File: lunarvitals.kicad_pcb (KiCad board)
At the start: 2 copper layers, 48.5 x 35 mm, 38 parts, among them J1 ConductiveCord, J2 MPU6050, J3 SEN11574, J4 MAX30102, J5 USB_C_Receptacle_PowerOnly_6P, J6 Battery, J7 Conn_01x07, Q1 FS8205, SW1 SW_SPDT, U1 NRF52840-DONGLE, U3 AP2112K-3.3, U4 TP4056, U5 MLX90614ESF-AAA-000-TU, U6 DW01A

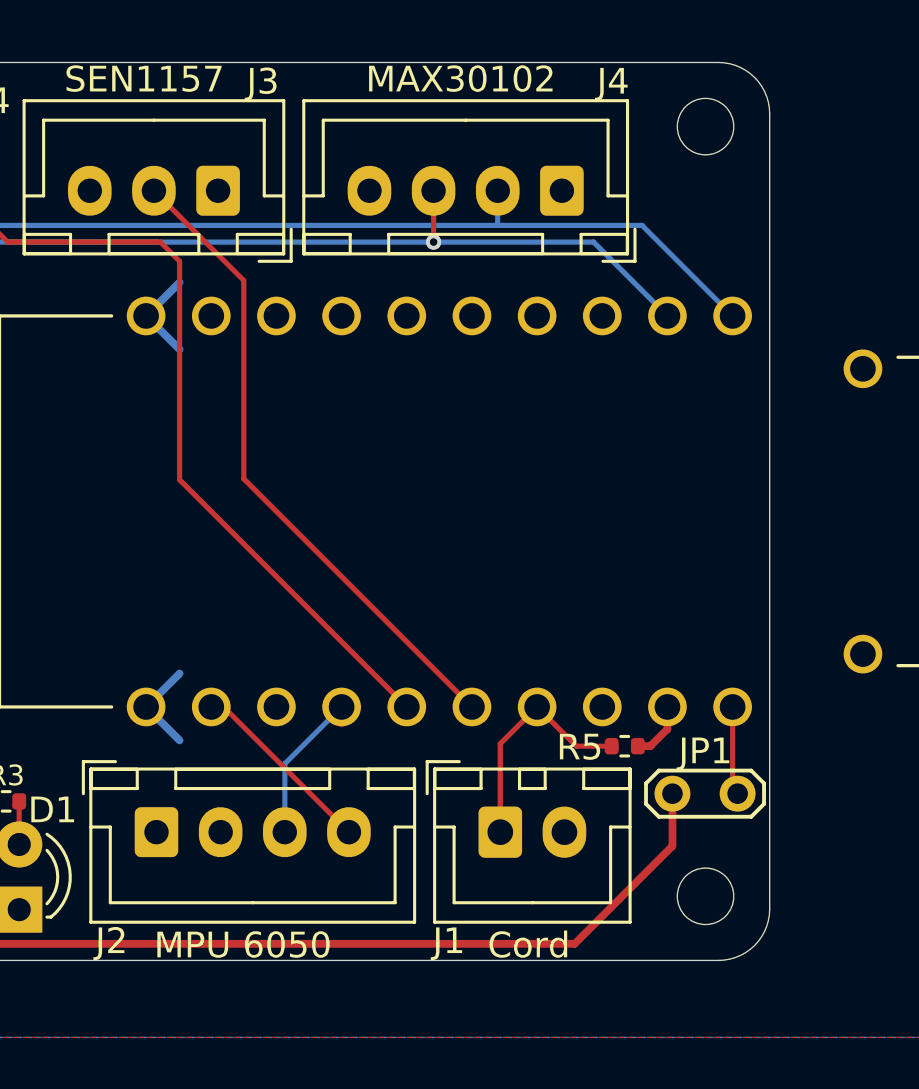
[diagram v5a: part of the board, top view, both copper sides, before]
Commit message: added unpopulated pullup resistors for I2C
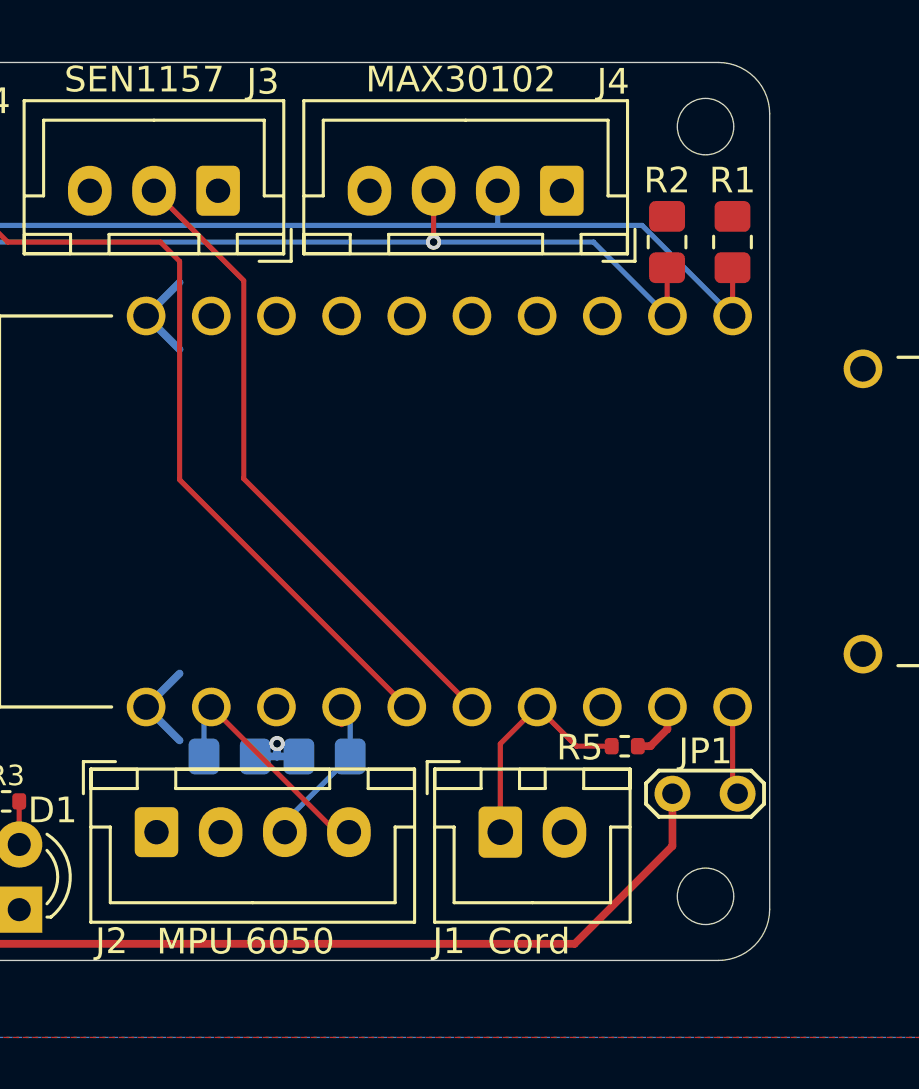
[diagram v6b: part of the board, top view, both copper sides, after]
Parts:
- added R1: R, Resistor_SMD:R_0805_2012Metric_Pad1.20x1.40mm_HandSolder, F.Cu at (188.1, 99.5)
- added R11: R, Resistor_SMD:R_0805_2012Metric_Pad1.20x1.40mm_HandSolder, B.Cu at (172.2, 119.5)
- added R2: R, Resistor_SMD:R_0805_2012Metric_Pad1.20x1.40mm_HandSolder, F.Cu at (185.5, 99.5)
- added R6: R, Resistor_SMD:R_0805_2012Metric_Pad1.20x1.40mm_HandSolder, B.Cu at (168.4, 119.5)
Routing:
- net +3.3V: track 11.1 -> 13.3 mm, vias 0 -> 1
- net /I2C1_SDA: track 7.39 -> 9.43 mm
- net /I2C0_SCL: track 48.5 -> 50.4 mm
- net /I2C0_SDA: track 46.5 -> 48.3 mm

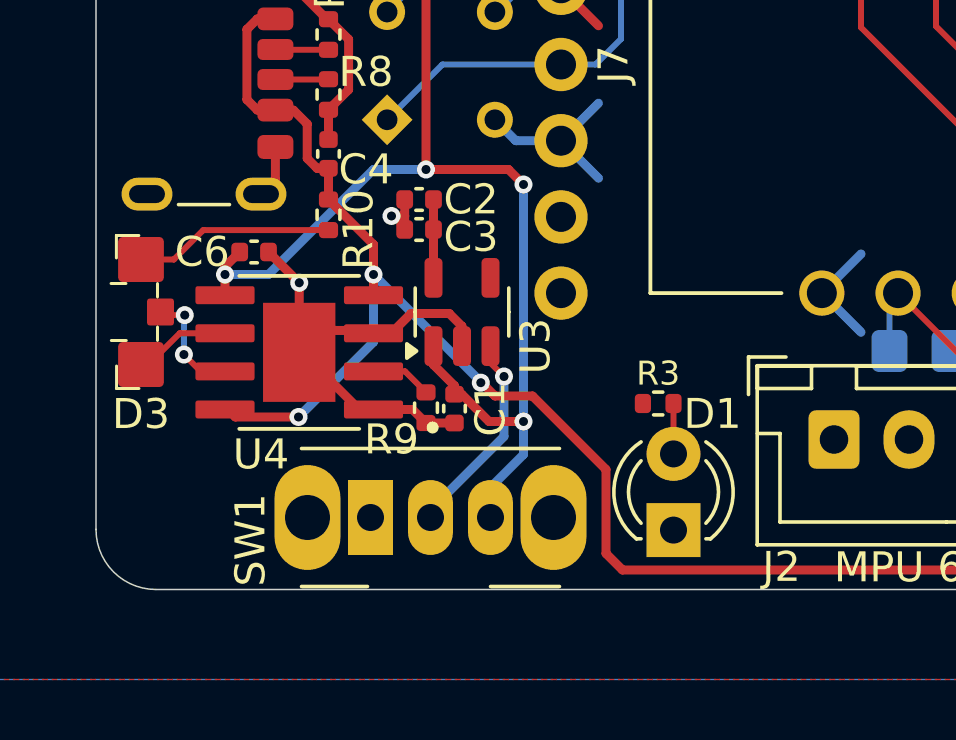
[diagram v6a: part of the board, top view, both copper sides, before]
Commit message: reorient LED through holes
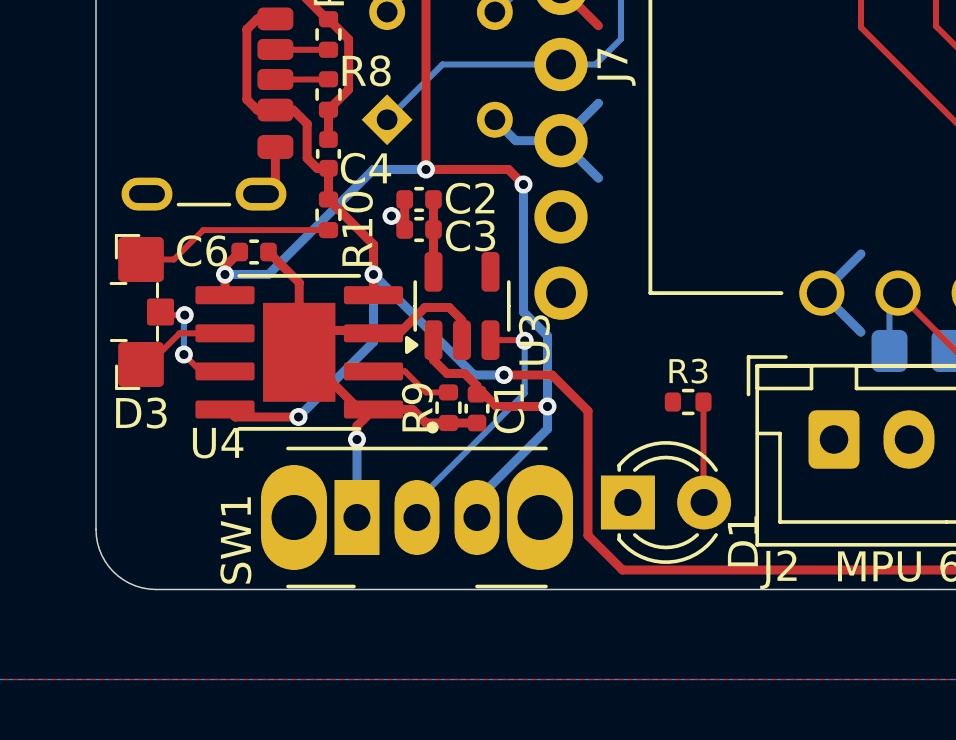
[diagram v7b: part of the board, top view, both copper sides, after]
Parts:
- moved D1 1.78 mm to (158.7, 124.6), turned to 0 degrees
- moved R3 1.00 mm to (160.7, 121.2)
- moved C1 0.75 mm to (153.7, 121.5)
- moved R9 0.75 mm to (152.8, 121.4)
- moved SW1 0.45 mm to (149.7, 125.1)
- moved U3 0.20 mm to (153.2, 118.0)
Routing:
- net GND: track 48.6 -> 51.9 mm
- net Net-(D1-A): track 1.68 -> 3.36 mm
- net BOut+: track 51.0 -> 52.5 mm
- net Net-(SW1-B): track 7.41 -> 8.53 mm
- net +5V: track 66.4 -> 67.2 mm
- net Net-(U4-PROG): track 2.60 -> 3.10 mm

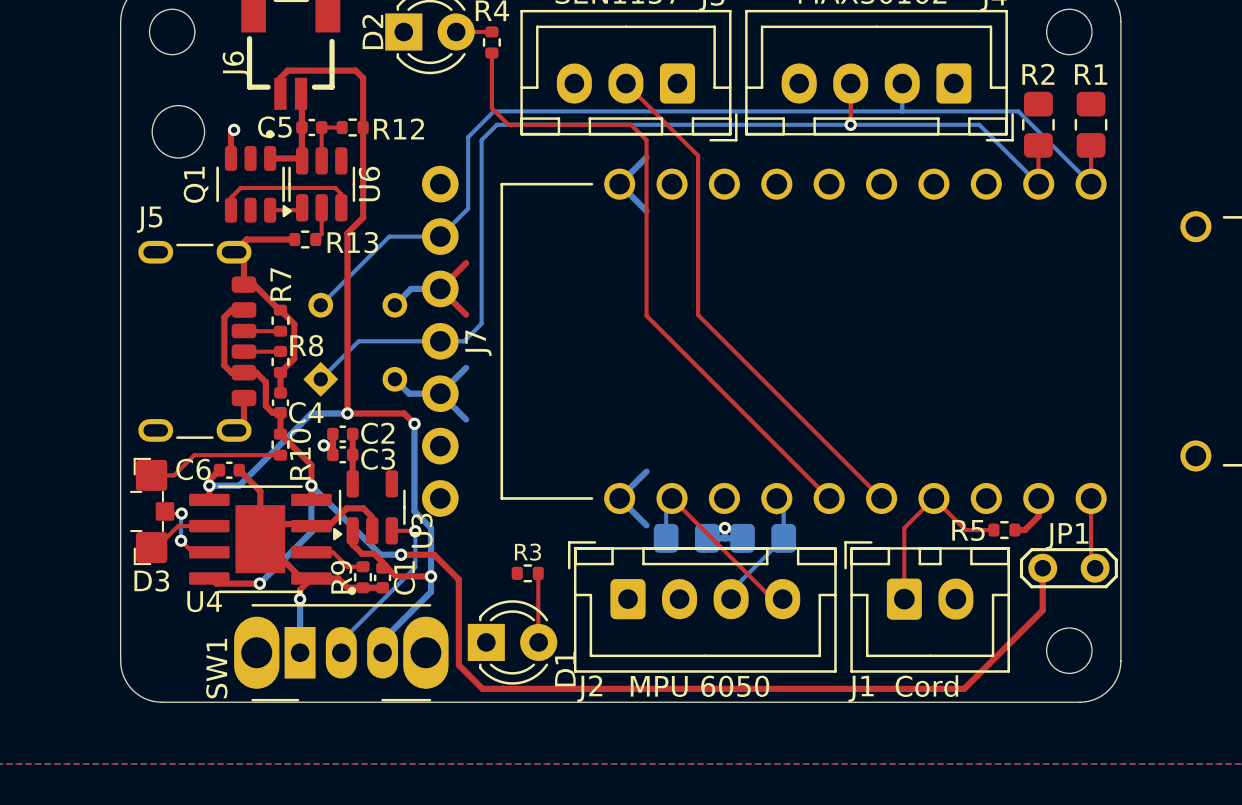
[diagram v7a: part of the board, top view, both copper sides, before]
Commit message: fix jumper footprint and adjust charge indication led
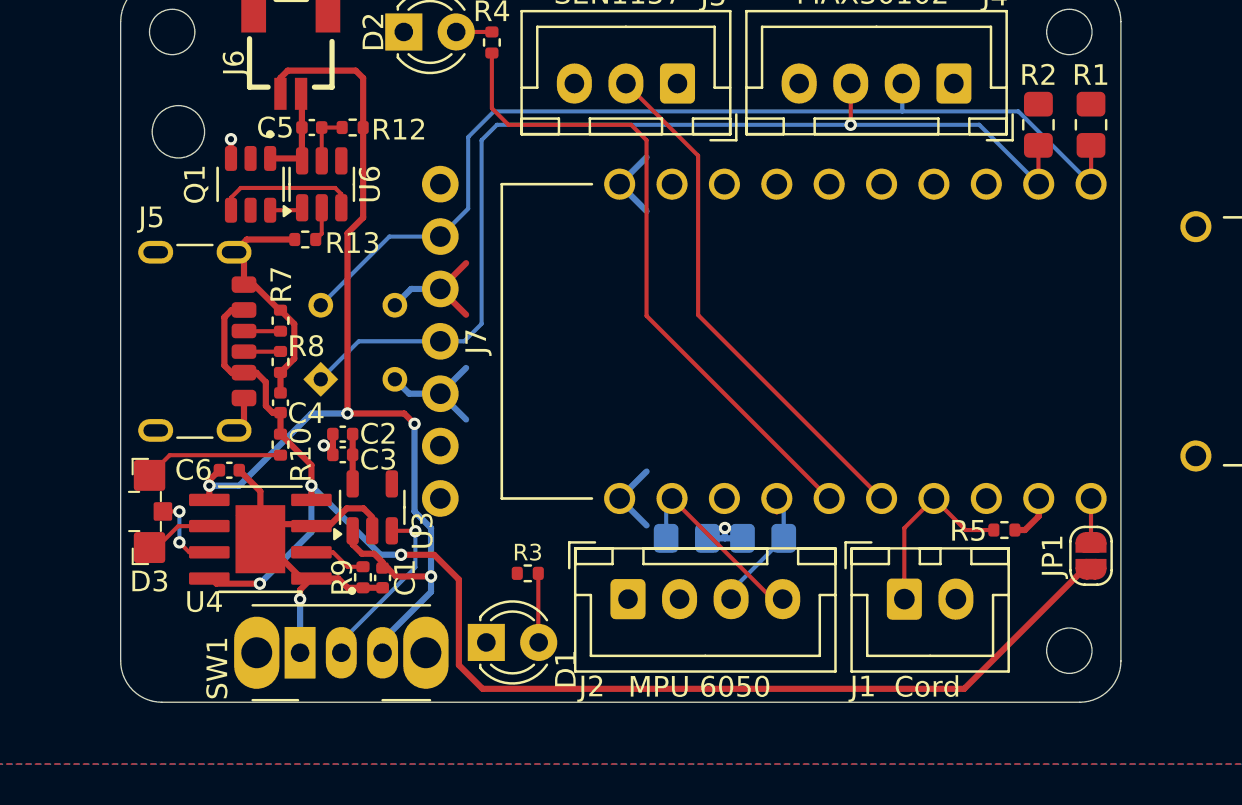
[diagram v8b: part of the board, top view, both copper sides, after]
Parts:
- JP1: footprint TestPoint:TestPoint_2Pads_Pitch2.54mm_Drill0.8mm -> Jumper:SolderJumper-2_P1.3mm_Open_RoundedPad1.0x1.5mm
- moved JP1 0.63 mm to (188.1, 120.4), turned to -90 degrees
- moved D3 0.10 mm to (142.4, 118.2)
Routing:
- net Net-(JP1-A): track 3.46 -> 2.13 mm
- net +5V: track 67.2 -> 68.3 mm
- net GND: track 51.9 -> 51.4 mm
